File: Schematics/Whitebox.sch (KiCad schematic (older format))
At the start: 3 parts, among them SW1 SW_Push

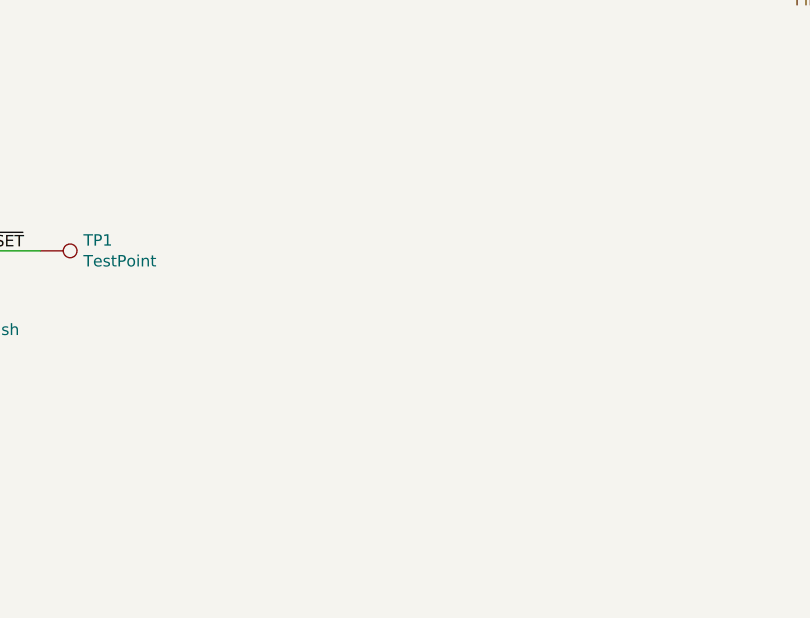
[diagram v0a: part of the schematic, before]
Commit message: Finished initial component placement
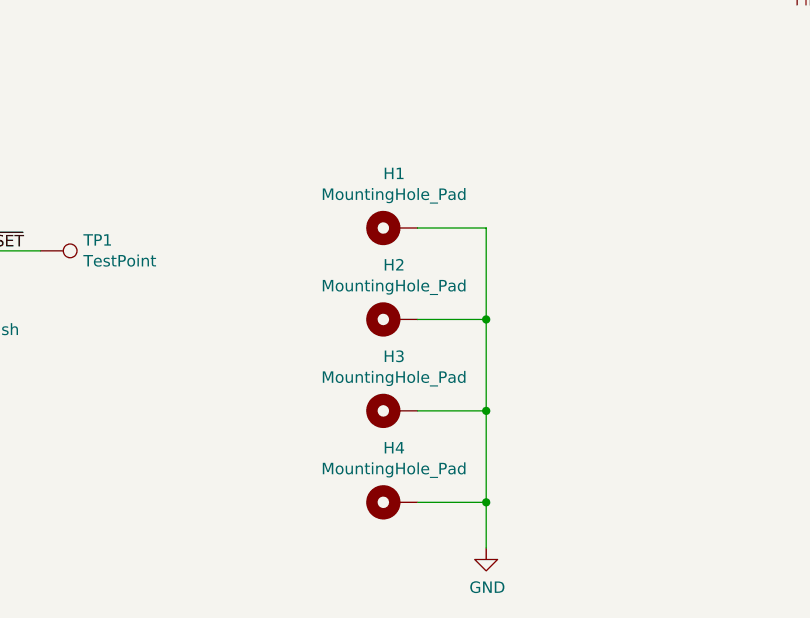
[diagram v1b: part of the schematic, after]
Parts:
- added H1, H2, H3, H4: MountingHole_Pad, MountingHole:MountingHole_2.2mm_M2_Pad, symbol Mechanical:MountingHole_Pad
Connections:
- net GND: now also H1.1, H2.1, H3.1, H4.1
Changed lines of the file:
@@
 Wire Wire Line
 	2250 5350 2800 5350
+$Comp
+L Mechanical:MountingHole_Pad H1
+U 1 1 5F2030DC
+P 4800 5250
+F 0 "H1" V 5037 5253 50  0000 C CNN
+F 1 "MountingHole_Pad" V 4946 5253 50  0000 C CNN
+F 2 "MountingHole:MountingHole_2.2mm_M2_Pad" H 4800 5250 50  0001 C CNN
+F 3 "~" H 4800 5250 50  0001 C CNN
+	1    4800 5250
+	0    -1   -1   0
+$EndComp
+$Comp
+L Mechanical:MountingHole_Pad H2
+U 1 1 5F20378E
+P 4800 5650
+F 0 "H2" V 5037 5653 50  0000 C CNN
+F 1 "MountingHole_Pad" V 4946 5653 50  0000 C CNN
+F 2 "MountingHole:MountingHole_2.2mm_M2_Pad" H 4800 5650 50  0001 C CNN
+F 3 "~" H 4800 5650 50  0001 C CNN
+	1    4800 5650
+	0    -1   -1   0
+$EndComp
+$Comp
+L Mechanical:MountingHole_Pad H3
+U 1 1 5F204455
+P 4800 6050
+F 0 "H3" V 5037 6053 50  0000 C CNN
+F 1 "MountingHole_Pad" V 4946 6053 50  0000 C CNN
+F 2 "MountingHole:MountingHole_2.2mm_M2_Pad" H 4800 6050 50  0001 C CNN
+F 3 "~" H 4800 6050 50  0001 C CNN
+	1    4800 6050
+	0    -1   -1   0
+$EndComp
+$Comp
+L Mechanical:MountingHole_Pad H4
+U 1 1 5F20445B
+P 4800 6450
+F 0 "H4" V 5037 6453 50  0000 C CNN
+F 1 "MountingHole_Pad" V 4946 6453 50  0000 C CNN
+F 2 "MountingHole:MountingHole_2.2mm_M2_Pad" H 4800 6450 50  0001 C CNN
+F 3 "~" H 4800 6450 50  0001 C CNN
+	1    4800 6450
+	0    -1   -1   0
+$EndComp
+$Comp
+L power:GND #PWR093
+U 1 1 5F20465A
+P 5200 6650
+F 0 "#PWR093" H 5200 6400 50  0001 C CNN
+F 1 "GND" H 5205 6477 50  0000 C CNN
+F 2 "" H 5200 6650 50  0001 C CNN
+F 3 "" H 5200 6650 50  0001 C CNN
+	1    5200 6650
+	1    0    0    -1
+$EndComp
+Wire Wire Line
+	4900 5250 5200 5250
+Wire Wire Line
+	4900 5650 5200 5650
+Wire Wire Line
+	5200 5250 5200 5650
+Connection ~ 5200 5650
+Wire Wire Line
+	5200 5650 5200 6050
+Wire Wire Line
+	4900 6050 5200 6050
+Connection ~ 5200 6050
+Wire Wire Line
+	5200 6050 5200 6450
+Wire Wire Line
+	4900 6450 5200 6450
+Connection ~ 5200 6450
+Wire Wire Line
+	5200 6450 5200 6650
 $EndSCHEMATC
